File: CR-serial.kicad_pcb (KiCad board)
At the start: 2 copper layers, 55.6 x 40.6 mm, 26 parts, among them J1 USB, J2 GPIO, J3 UART0, J4 UART1, J5 UART2, J6 UART3_HV, J7 RS232_0, J8 RS232_1, U1 CP2108-xxx-xM, U2 MAX232

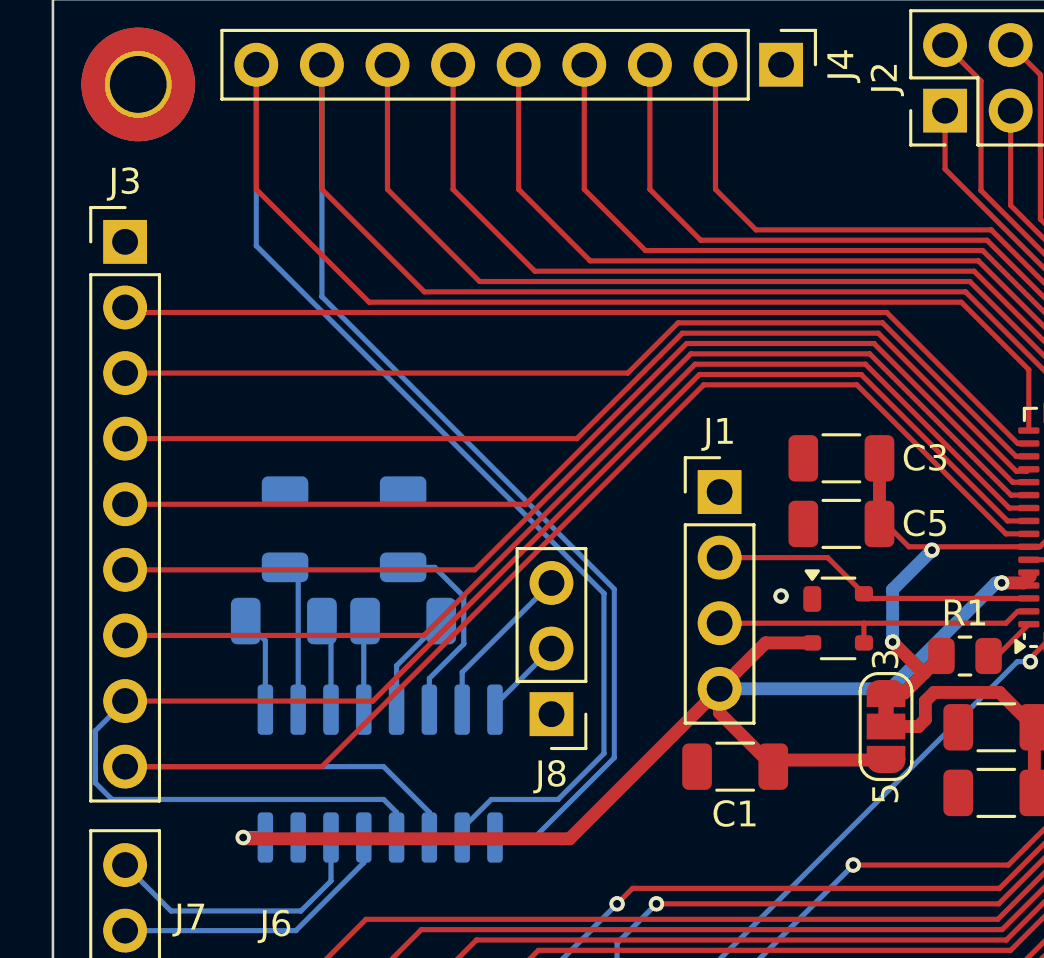
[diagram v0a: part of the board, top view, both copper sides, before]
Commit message: Move UART0 connector around
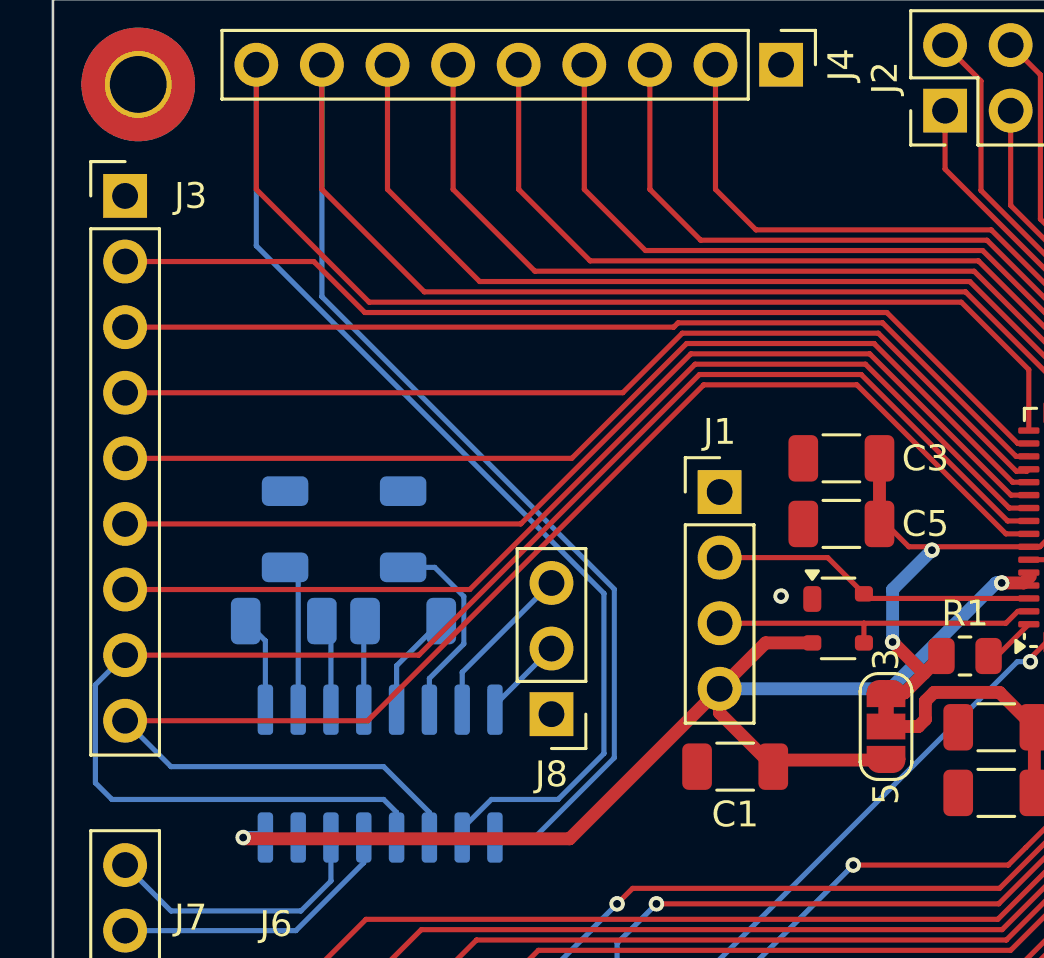
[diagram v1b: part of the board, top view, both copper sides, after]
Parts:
- moved J3 1.78 mm to (160.5, 104.1)
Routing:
- net /RX0: track 59.3 -> 60.4 mm
- net Net-(J3-Pin_7): track 41.7 -> 40.9 mm
- net Net-(J3-Pin_5): track 39.8 -> 39.1 mm
- net Net-(J3-Pin_3): track 37.9 -> 37.2 mm
- net Net-(J3-Pin_6): track 40.7 -> 40.0 mm
- net Net-(J3-Pin_2): track 37.2 -> 37.9 mm
- net Net-(J3-Pin_4): track 38.9 -> 38.2 mm
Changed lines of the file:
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@@
 	(footprint "Connector_PinHeader_2.54mm:PinHeader_1x09_P2.54mm_Vertical"
 		(layer "F.Cu")
-		(at 160.528 105.918)
+		(at 160.528 104.14)
 		(descr "Through hole straight pin header, 1x09, 2.54mm pitch, single row")
 		(tags "Through hole pin header THT 1x09 2.54mm single row")
 		(property "Reference" "J3"
-			(at 0 -2.33 0)
+			(at 2.54 0 0)
 			(layer "F.SilkS")
 			(effects
@@
 	)
 	(segment
-		(start 194.699498 116.7245)
-		(end 195.5205 116.7245)
+		(start 189.028998 111.054)
+		(end 194.699498 116.7245)
 		(width 0.2)
 		(layer "F.Cu")
@@
 	)
 	(segment
-		(start 182.766314 111.054)
-		(end 189.028998 111.054)
+		(start 160.528 121.92)
+		(end 171.900314 121.92)
 		(width 0.2)
 		(layer "F.Cu")
@@
 	)
 	(segment
-		(start 189.028998 111.054)
-		(end 194.699498 116.7245)
+		(start 171.900314 121.92)
+		(end 182.766314 111.054)
 		(width 0.2)
 		(layer "F.Cu")
@@
 	)
 	(segment
-		(start 160.528 123.698)
-		(end 170.122314 123.698)
+		(start 194.699498 116.7245)
+		(end 195.5205 116.7245)
 		(width 0.2)
 		(layer "F.Cu")
@@
 	)
 	(segment
-		(start 170.122314 123.698)
-		(end 182.766314 111.054)
+		(start 182.766314 111.054)
+		(end 189.028998 111.054)
 		(width 0.2)
 		(layer "F.Cu")
@@
 	)
 	(segment
-		(start 159.378 124.848)
-		(end 160.528 123.698)
-		(width 0.2)
-		(layer "B.Cu")
-		(net 29)
-	)
-	(segment
-		(start 171.04 128.008001)
-		(end 170.539999 127.508)
+		(start 160.02 127.508)
+		(end 159.378 126.866)
 		(width 0.2)
 		(layer "B.Cu")
@@
 	)
 	(segment
-		(start 160.02 127.508)
-		(end 159.378 126.866)
+		(start 170.539999 127.508)
+		(end 160.02 127.508)
 		(width 0.2)
 		(layer "B.Cu")
@@
 	)
 	(segment
-		(start 170.539999 127.508)
-		(end 160.02 127.508)
+		(start 159.378 123.07)
+		(end 160.528 121.92)
 		(width 0.2)
 		(layer "B.Cu")
@@
 	(segment
 		(start 159.378 126.866)
-		(end 159.378 124.848)
+		(end 159.378 123.07)
 		(width 0.2)
 		(layer "B.Cu")
@@
 	)
 	(segment
-		(start 182.600628 110.654)
-		(end 189.194684 110.654)
+		(start 171.04 128.008001)
+		(end 170.539999 127.508)
 		(width 0.2)
-		(layer "F.Cu")
-		(net 30)
+		(layer "B.Cu")
+		(net 29)
 	)
 	(segment
@@
 	)
 	(segment
-		(start 160.528 121.158)
-		(end 172.096628 121.158)
+		(start 173.874628 119.38)
+		(end 182.600628 110.654)
 		(width 0.2)
 		(layer "F.Cu")
@@
 	)
 	(segment
-		(start 172.096628 121.158)
-		(end 182.600628 110.654)
+		(start 182.600628 110.654)
+		(end 189.194684 110.654)
 		(width 0.2)
 		(layer "F.Cu")
@@
 	)
 	(segment
-		(start 189.691742 109.454)
-		(end 195.037242 114.7995)
+		(start 160.528 119.38)
+		(end 173.874628 119.38)
+		(width 0.2)
+		(layer "F.Cu")
+		(net 30)
+	)
+	(segment
+		(start 160.528 111.76)
+		(end 179.79757 111.76)
 		(width 0.2)
 		(layer "F.Cu")
@@
 	)
 	(segment
-		(start 182.10357 109.454)
-		(end 189.691742 109.454)
+		(start 189.691742 109.454)
+		(end 195.037242 114.7995)
 		(width 0.2)
 		(layer "F.Cu")
@@
 	)
 	(segment
-		(start 160.528 113.538)
-		(end 178.01957 113.538)
+		(start 182.10357 109.454)
+		(end 189.691742 109.454)
 		(width 0.2)
 		(layer "F.Cu")
@@
 	)
 	(segment
-		(start 178.01957 113.538)
+		(start 179.79757 111.76)
 		(end 182.10357 109.454)
 		(width 0.2)
@@
 	)
 	(segment
-		(start 195.093614 113.7245)
-		(end 195.5205 113.7245)
+		(start 169.810314 108.654)
+		(end 190.023114 108.654)
 		(width 0.2)
 		(layer "F.Cu")
@@
 	)
 	(segment
-		(start 160.724 108.654)
-		(end 190.023114 108.654)
+		(start 160.528 106.68)
+		(end 167.836314 106.68)
 		(width 0.2)
 		(layer "F.Cu")
@@
 	)
 	(segment
-		(start 190.023114 108.654)
-		(end 195.093614 113.7245)
+		(start 167.836314 106.68)
+		(end 169.810314 108.654)
 		(width 0.2)
 		(layer "F.Cu")
@@
 	)
 	(segment
-		(start 160.528 108.458)
-		(end 160.724 108.654)
+		(start 190.023114 108.654)
+		(end 195.093614 113.7245)
 		(width 0.2)
 		(layer "F.Cu")
@@
 	)
 	(segment
-		(start 182.434942 110.254)
-		(end 189.36037 110.254)
+		(start 195.093614 113.7245)
+		(end 195.5205 113.7245)
 		(width 0.2)
 		(layer "F.Cu")
-		(net 33)
+		(net 32)
 	)
 	(segment
@@
 	)
 	(segment
-		(start 174.070942 118.618)
-		(end 182.434942 110.254)
+		(start 160.528 116.84)
+		(end 175.848942 116.84)
 		(width 0.2)
 		(layer "F.Cu")
@@
 	)
 	(segment
-		(start 160.528 118.618)
-		(end 174.070942 118.618)
+		(start 182.434942 110.254)
+		(end 189.36037 110.254)
 		(width 0.2)
 		(layer "F.Cu")
@@
 	)
 	(segment
-		(start 168.148 126.238)
-		(end 182.932 111.454)
+		(start 175.848942 116.84)
+		(end 182.434942 110.254)
 		(width 0.2)
 		(layer "F.Cu")
-		(net 34)
+		(net 33)
 	)
 	(segment
-		(start 188.863312 111.454)
-		(end 194.633812 117.2245)
+		(start 194.633812 117.2245)
+		(end 195.5205 117.2245)
 		(width 0.2)
 		(layer "F.Cu")
@@
 	)
 	(segment
-		(start 194.633812 117.2245)
-		(end 195.5205 117.2245)
+		(start 160.528 124.46)
+		(end 169.926 124.46)
 		(width 0.2)
 		(layer "F.Cu")
@@
 	)
 	(segment
-		(start 160.528 126.238)
-		(end 168.148 126.238)
+		(start 169.926 124.46)
+		(end 182.932 111.454)
 		(width 0.2)
 		(layer "F.Cu")
@@
 	)
 	(segment
+		(start 188.863312 111.454)
+		(end 194.633812 117.2245)
+		(width 0.2)
+		(layer "F.Cu")
+		(net 34)
+	)
+	(segment
+		(start 170.539999 126.238)
+		(end 162.306 126.238)
+		(width 0.2)
+		(layer "B.Cu")
+		(net 34)
+	)
+	(segment
+		(start 162.306 126.238)
+		(end 160.528 124.46)
+		(width 0.2)
+		(layer "B.Cu")
+		(net 34)
+	)
+	(segment
 		(start 172.31 128.983)
 		(end 172.31 128.008001)
@@
 	)
 	(segment
-		(start 170.539999 126.238)
-		(end 160.528 126.238)
+		(start 189.857428 109.054)
+		(end 195.027928 114.2245)
 		(width 0.2)
-		(layer "B.Cu")
-		(net 34)
+		(layer "F.Cu")
+		(net 35)
 	)
 	(segment
@@
 	)
 	(segment
-		(start 160.528 110.998)
-		(end 179.993884 110.998)
+		(start 181.937884 109.054)
+		(end 189.857428 109.054)
 		(width 0.2)
 		(layer "F.Cu")
@@
 	)
 	(segment
-		(start 179.993884 110.998)
+		(start 181.771884 109.22)
 		(end 181.937884 109.054)
 		(width 0.2)
@@
 	)
 	(segment
-		(start 181.937884 109.054)
-		(end 189.857428 109.054)
+		(start 160.528 109.22)
+		(end 181.771884 109.22)
 		(width 0.2)
 		(layer "F.Cu")
@@
 	)
 	(segment
-		(start 189.857428 109.054)
-		(end 195.027928 114.2245)
+		(start 160.528 114.3)
+		(end 177.823256 114.3)
 		(width 0.2)
 		(layer "F.Cu")
-		(net 35)
+		(net 36)
 	)
 	(segment
-		(start 182.269256 109.854)
-		(end 189.526056 109.854)
+		(start 194.896556 115.2245)
+		(end 195.5205 115.2245)
 		(width 0.2)
 		(layer "F.Cu")
@@
 	)
 	(segment
-		(start 160.528 116.078)
-		(end 176.045256 116.078)
+		(start 177.823256 114.3)
+		(end 182.269256 109.854)
 		(width 0.2)
 		(layer "F.Cu")
@@
 	)
 	(segment
-		(start 194.896556 115.2245)
-		(end 195.5205 115.2245)
-		(width 0.2)
-		(layer "F.Cu")
-		(net 36)
-	)
-	(segment
-		(start 176.045256 116.078)
-		(end 182.269256 109.854)
+		(start 182.269256 109.854)
+		(end 189.526056 109.854)
 		(width 0.2)
 		(layer "F.Cu")

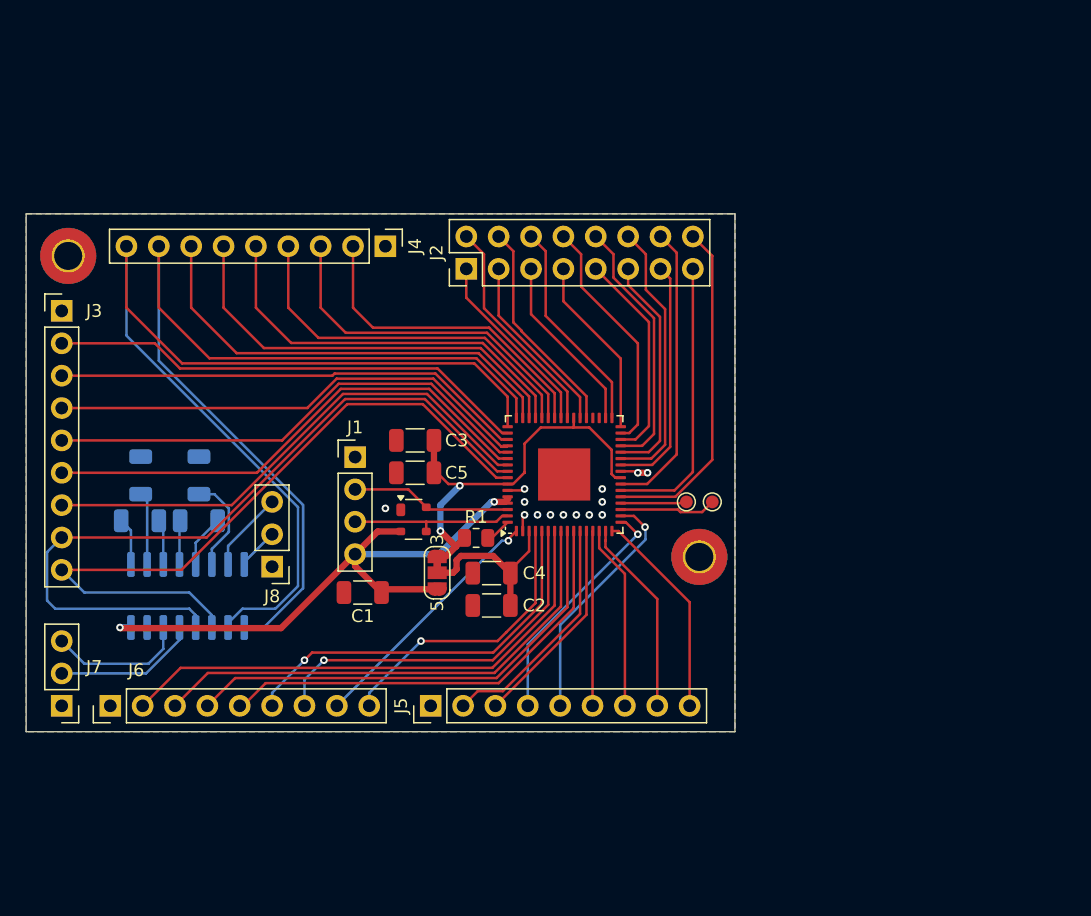
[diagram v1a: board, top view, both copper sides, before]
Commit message: Extend board, move UART2-3 around
(Areas unfilled...)
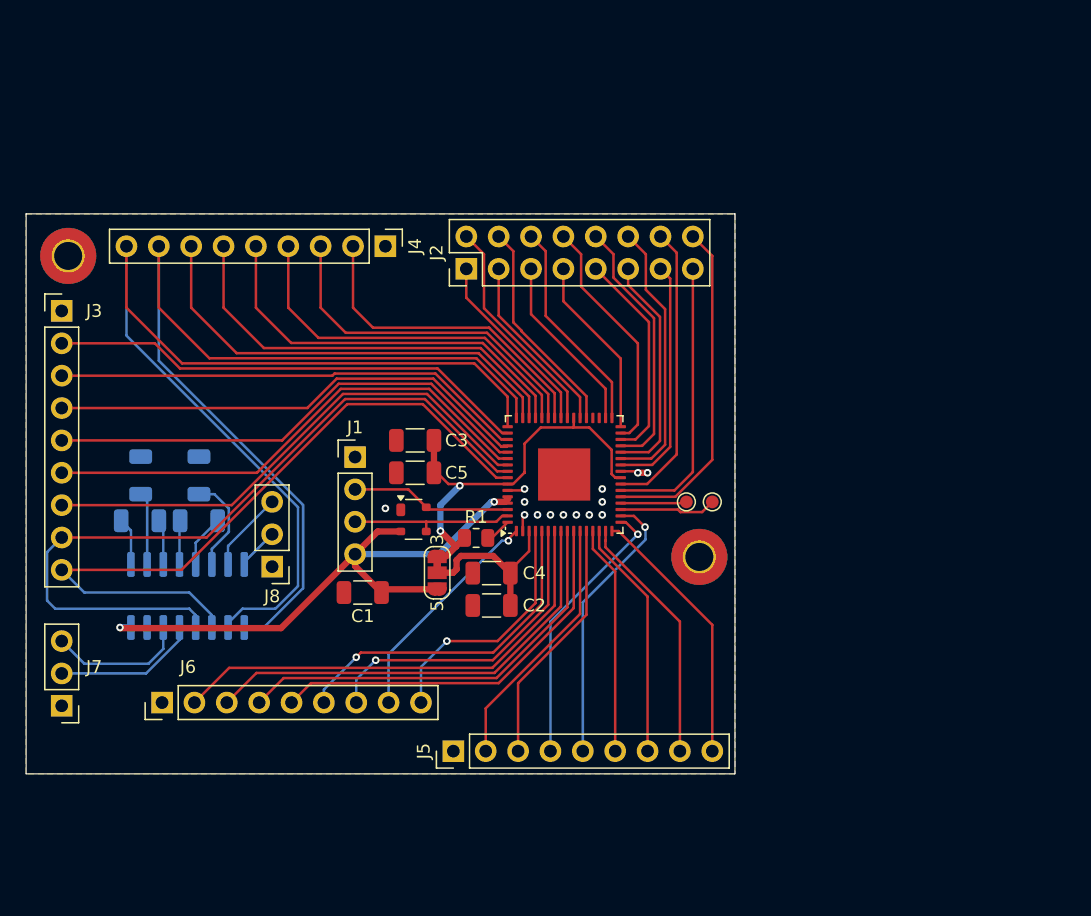
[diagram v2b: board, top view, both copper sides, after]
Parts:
- moved J6 4.07 mm to (168.4, 134.9)
- moved J5 3.98 mm to (191.3, 138.7)
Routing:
- net Net-(J6-Pin_7): track 29.4 -> 25.1 mm
- net Net-(J5-Pin_7): track 14.6 -> 18.8 mm
- net Net-(J5-Pin_9): track 16.5 -> 20.8 mm
- net Net-(J5-Pin_8): track 15.4 -> 19.7 mm
- net Net-(J5-Pin_6): track 13.7 -> 18.0 mm
- net Net-(J6-Pin_6): track 30.8 -> 26.6 mm
- net Net-(J6-Pin_5): track 35.4 -> 31.3 mm
- net Net-(J6-Pin_2): track 41.4 -> 37.3 mm
- net Net-(J6-Pin_4): track 37.4 -> 33.3 mm
- net Net-(J6-Pin_3): track 39.4 -> 35.3 mm
- net Net-(J6-Pin_9): track 22.6 -> 19.5 mm
- net Net-(J5-Pin_5): track 19.1 -> 21.9 mm
- net Net-(J5-Pin_4): track 18.8 -> 21.6 mm
- net Net-(J5-Pin_3): track 16.7 -> 19.5 mm
- net Net-(J6-Pin_8): track 19.8 -> 17.9 mm
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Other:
- board size 55.6 x 40.6 mm -> 55.6 x 43.9 mm

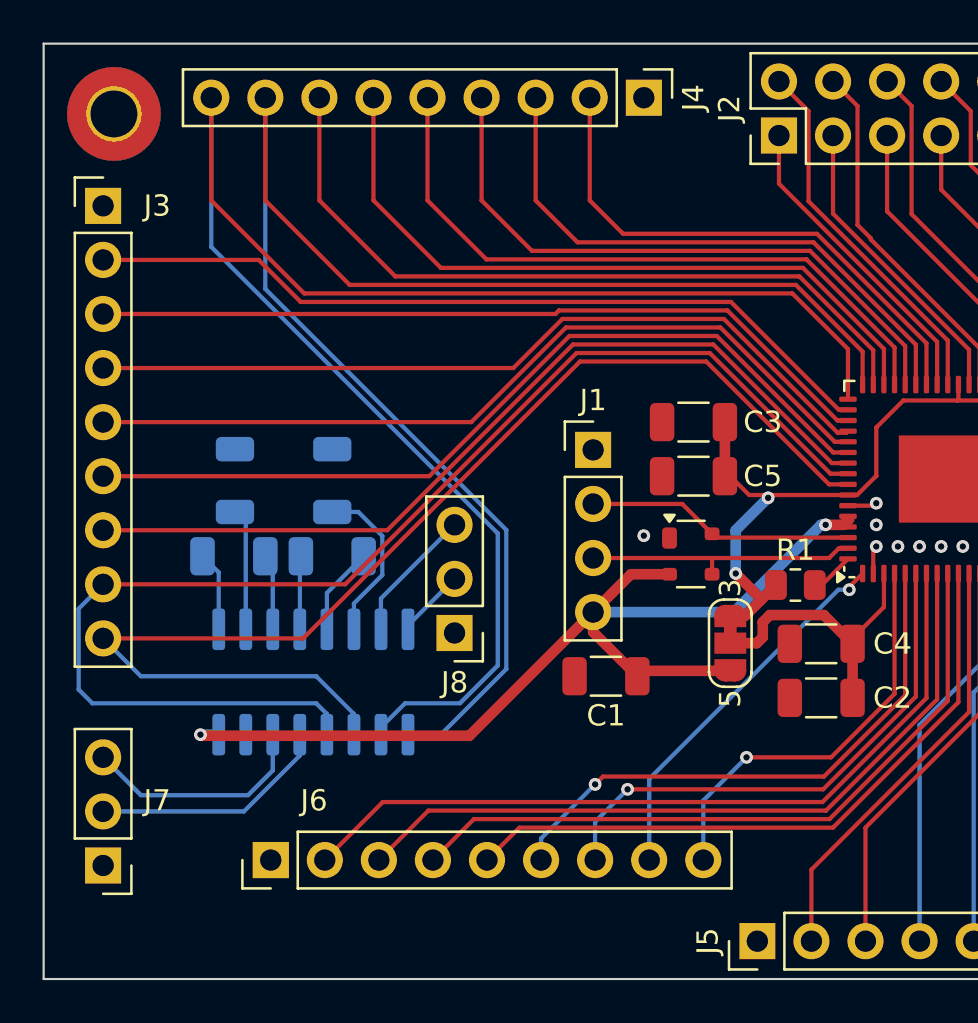
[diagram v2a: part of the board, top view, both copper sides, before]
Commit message: Change RS232 connectors
Zones filled again
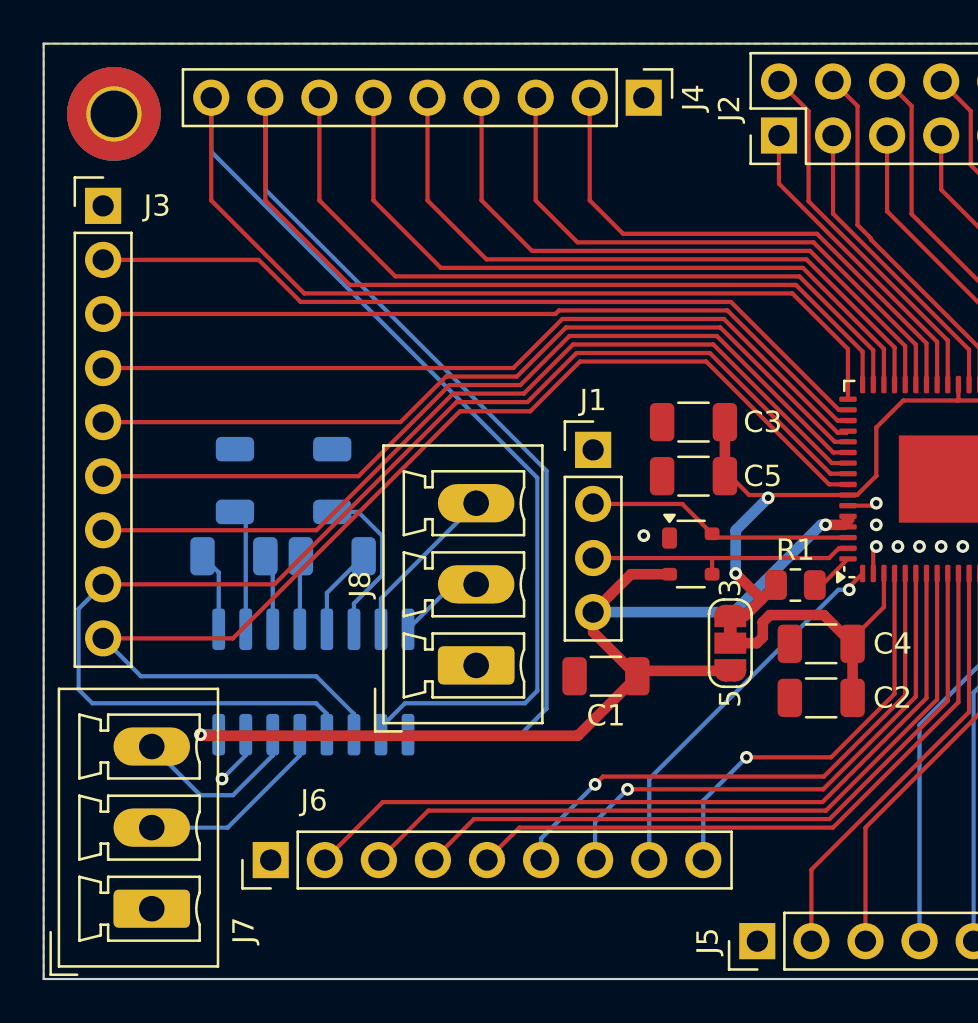
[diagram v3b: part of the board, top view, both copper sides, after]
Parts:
- J7, J8: footprint Connector_PinHeader_2.54mm:PinHeader_1x03_P2.54mm_Vertical -> Connector_Phoenix_MC:PhoenixContact_MCV_1,5_3-G-3.81_1x03_P3.81mm_Vertical
- moved J7 3.06 mm to (162.8, 137.2), turned to 90 degrees
- moved J8 1.83 mm to (178.1, 125.7), turned to 90 degrees
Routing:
- net /RX1: track 74.8 -> 78.6 mm
- net /TX1: track 79.3 -> 82.6 mm
- net GND: track 4.86 -> 7.40 mm, vias 14 -> 15
- net Net-(J7-Pin_3): track 10.9 -> 8.38 mm
- net Net-(J7-Pin_2): track 11.3 -> 9.34 mm
- net Net-(J8-Pin_3): track 6.34 -> 7.78 mm
- net VBUS: track 48.2 -> 49.1 mm
- net Net-(J8-Pin_2): track 3.27 -> 4.08 mm
